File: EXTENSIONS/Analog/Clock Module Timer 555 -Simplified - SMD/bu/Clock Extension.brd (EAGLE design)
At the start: 20 x 54 mm, 10 parts, among them X1 USB-A

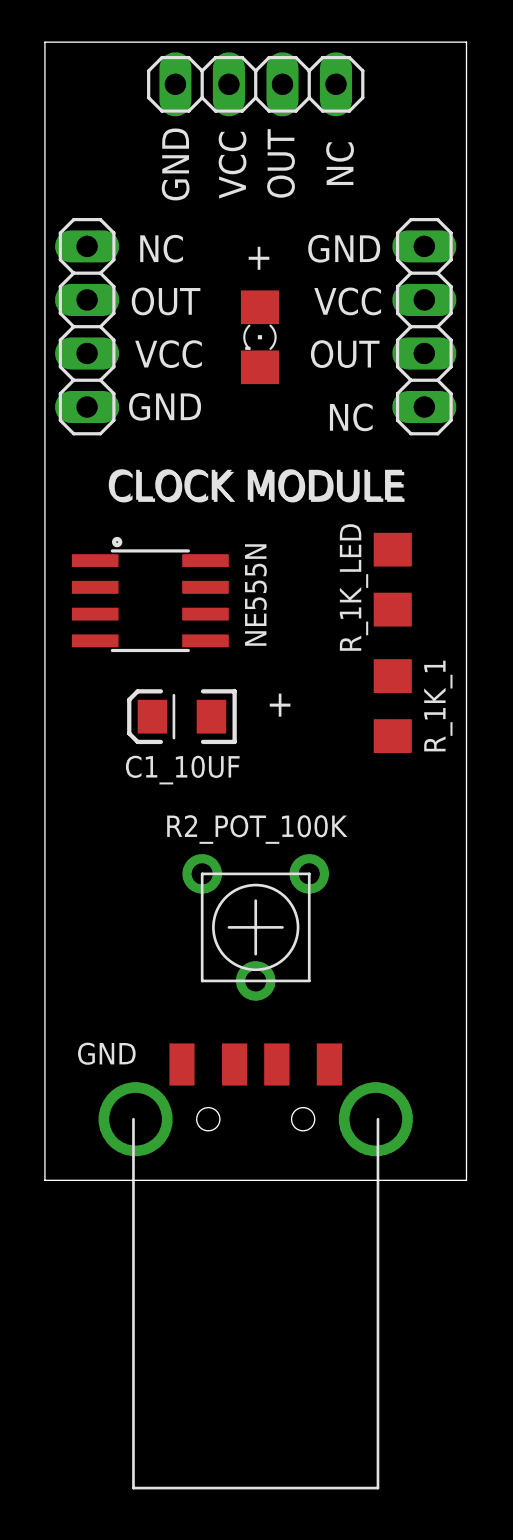
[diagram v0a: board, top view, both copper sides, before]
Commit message: Turn clock smd into a mounting pcb on top of a main pcb
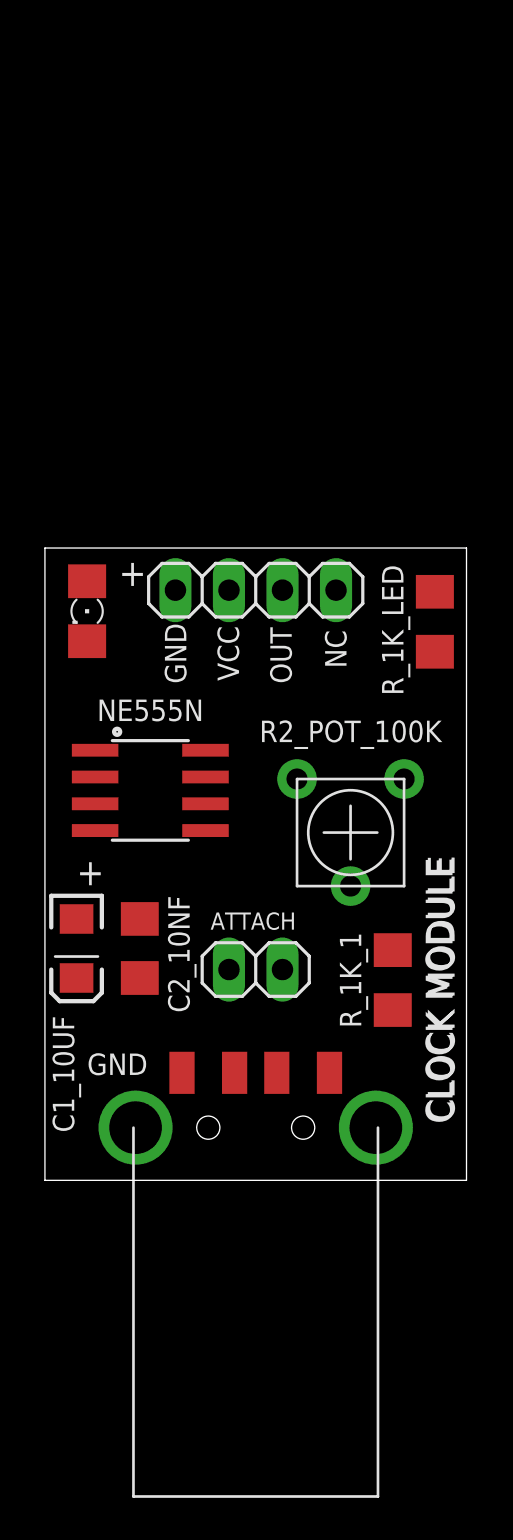
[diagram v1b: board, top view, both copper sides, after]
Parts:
- removed OUT_2, OUT_3: (no value), pinhead:1X04
- added ATTACH: (no value), pinhead:1X02
- added C2_10NF: (no value), adafruit:C1206
- moved OUT_1 24.0 mm to (12.0, 40.0)
- moved LED_OUTPUT 15.4 mm to (4.00, 39.0)
- moved R_1K_1 13.0 mm to (18.5, 21.5)
- moved C1_10UF 12.1 mm to (3.50, 23.0), turned to 270 degrees
- moved NE555N 9.00 mm to (7.00, 30.5)
- moved R2_POT_100K 6.36 mm to (16.5, 28.5)
- moved R_1K_LED 2.83 mm to (20.5, 38.5)
- moved X1 0.40 mm to (12.0, 14.5)
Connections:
- new net CONTROL: C2_10NF.2, NE555N.5
- net GND: now also C2_10NF.1; no longer OUT_2.1, OUT_3.1
- net TMR555_OUTPUT: no longer OUT_2.3, OUT_3.3
- net VCC: no longer OUT_2.2, OUT_3.2
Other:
- board size 20 x 54 mm -> 20 x 30 mm
